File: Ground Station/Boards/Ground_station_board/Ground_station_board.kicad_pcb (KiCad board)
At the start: 4 copper layers, 59.4 x 38.2 mm, 70 parts, among them J3 USB_B_Micro, J4 SWD JST PH, J5 MICROFIT, J6 RFIO SMA, U2 SX1262, U3 PE4259 RF Switch, U4 STM32H562RGT6, U5 MIC5365-3.3YC5, U6 MIC5365-3.3YC5, U7 AS78L05RTR-E1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

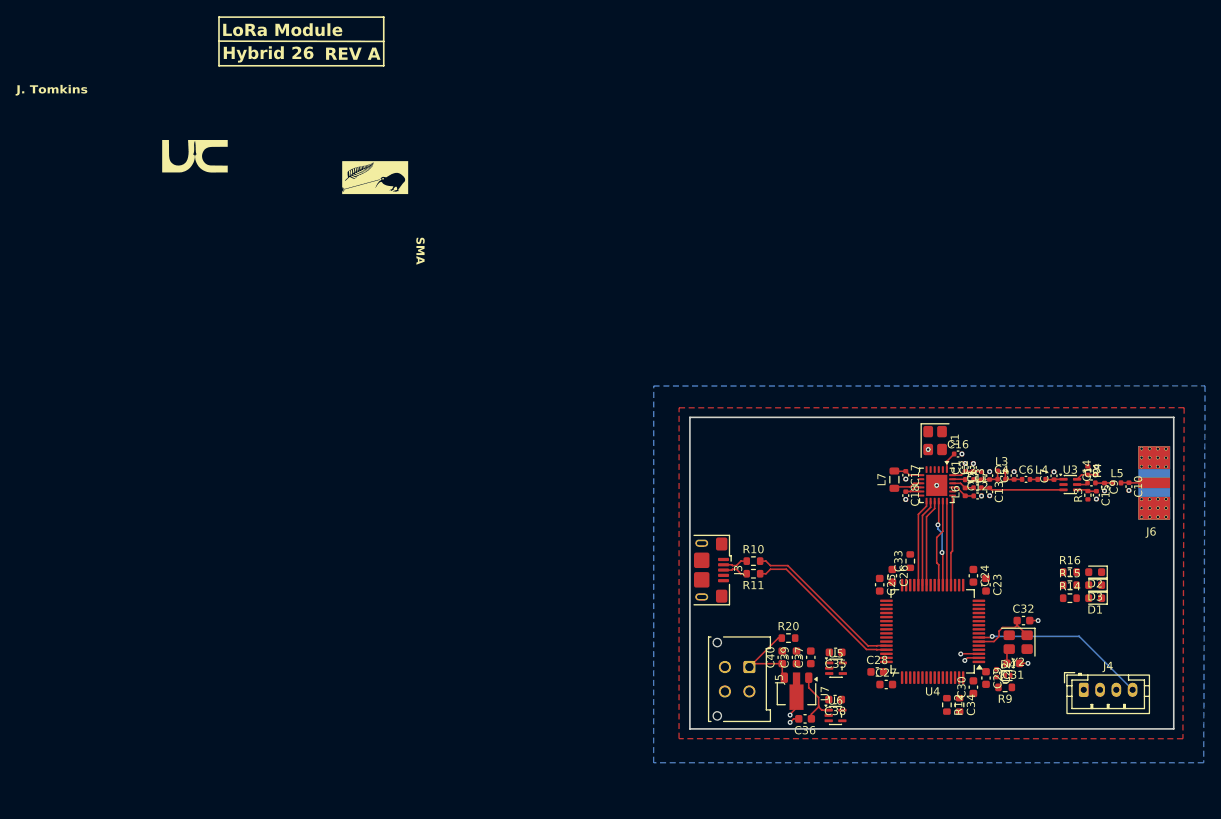
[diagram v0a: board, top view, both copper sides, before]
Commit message: via stitching added to gs board, need fencing before review
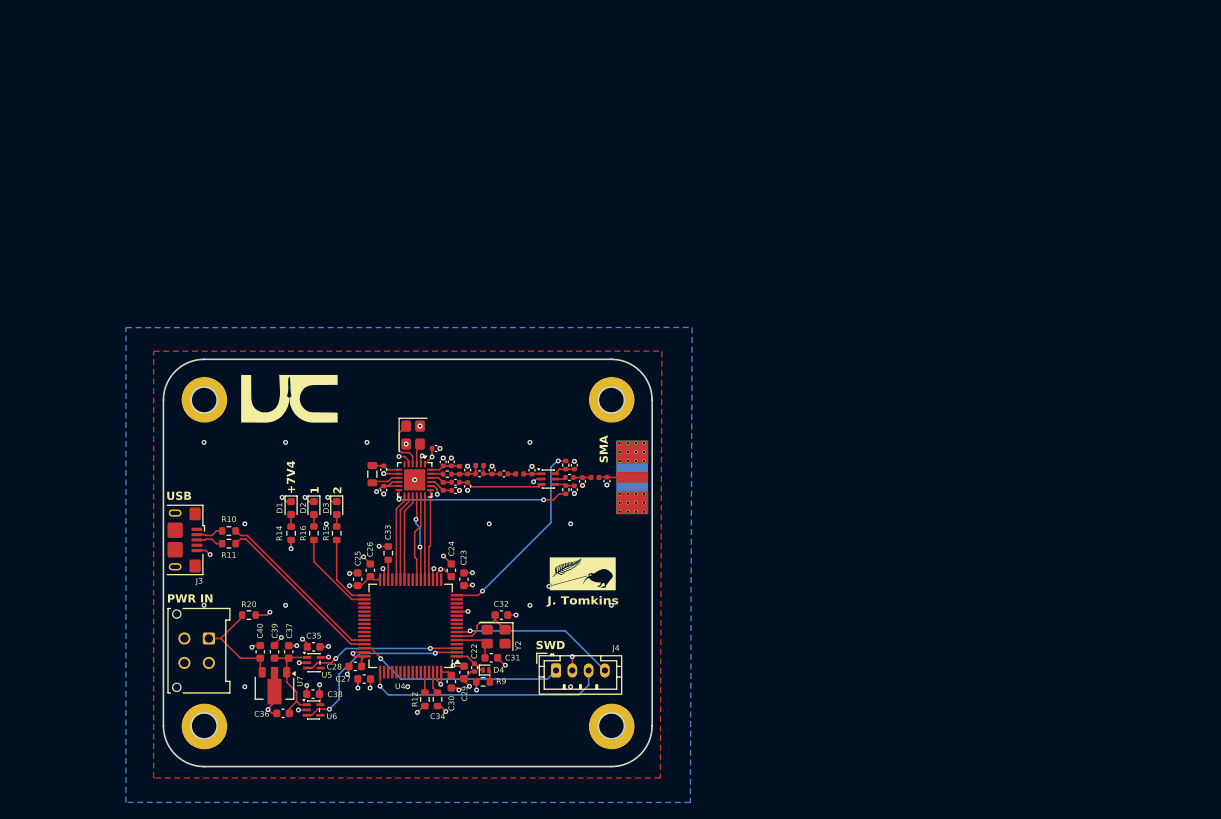
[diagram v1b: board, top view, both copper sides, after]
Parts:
- added H1: MountingHole, MountingHole:MountingHole_3.2mm_M3_DIN965_Pad, F.Cu at (125.1, 78.0)
- added H2: MountingHole, MountingHole:MountingHole_3.2mm_M3_DIN965_Pad, F.Cu at (175.1, 78.0)
- added H3: MountingHole, MountingHole:MountingHole_3.2mm_M3_DIN965_Pad, F.Cu at (125.1, 118.1)
- added H4: MountingHole, MountingHole:MountingHole_3.2mm_M3_DIN965_Pad, F.Cu at (175.1, 118.1)
- moved D1 99.3 mm to (135.7, 91.3), turned to -90 degrees
- moved D2 96.2 mm to (138.5, 91.3), turned to -90 degrees
- moved R14 95.9 mm to (135.7, 94.4), turned to 90 degrees
- moved D3 93.6 mm to (141.3, 91.3), turned to -90 degrees
- moved R16 92.9 mm to (138.5, 94.4), turned to 90 degrees
- moved R15 90.2 mm to (141.3, 94.4), turned to 90 degrees
- moved J5 66.5 mm to (125.6, 107.3)
- moved R20 66.3 mm to (130.6, 104.4)
- moved J4 64.8 mm to (168.3, 111.2)
- moved J3 64.8 mm to (121.5, 95.2)
- moved R10 64.5 mm to (128.1, 94.1)
- moved R11 64.5 mm to (128.1, 95.7)
- moved C33 64.1 mm to (147.7, 96.8)
- moved C1 64.1 mm to (154.4, 85.6)
- moved C10 64.1 mm to (174.5, 88.0)
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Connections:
- U4 pad 33: unconnected-(U4-PB12-Pad33) -> /MCU/LED1
- U4 pad 34: unconnected-(U4-PB13-Pad34) -> /MCU/LED2
- U4 pad 51: /MCU/LED2 -> unconnected-(U4-PC10-Pad51)
- U4 pad 52: /MCU/LED1 -> unconnected-(U4-PC11-Pad52)
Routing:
- net GND: track 8.12 -> 60.8 mm, vias 20 -> 65
- net /+3V3A: track 5.66 -> 44.5 mm, vias 0 -> 3
- net /MCU/SWDIO: track 0.00 -> 30.1 mm, vias 0 -> 1
- net /MCU/SWCLK: track 0.00 -> 25.6 mm, vias 0 -> 1
- net /LoRav2/ANT_SW: track 0.00 -> 24.2 mm, vias 0 -> 2
- net /LoRav2/DIO2: track 0.00 -> 22.0 mm, vias 0 -> 2
- net /MCU/3V3A_LDO_EN: track 1.86 -> 23.5 mm, vias 1 -> 2
- net /MCU/3V3_LDO_EN: track 2.24 -> 19.4 mm, vias 1 -> 2
- net +3V3: track 0.00 -> 12.3 mm, vias 0 -> 11
- net +7V4: track 0.00 -> 11.8 mm, vias 0 -> 2
- net /MCU/LED2: track 0.00 -> 10.8 mm
- net /MCU/LED1: track 0.00 -> 9.09 mm
- net /LoRav2/XTB: track 0.00 -> 6.27 mm
- net +5V: track 7.32 -> 13.2 mm
- net Net-(D4-K): track 0.00 -> 3.92 mm
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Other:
- board size 59.4 x 38.2 mm -> 60 x 50 mm
- board text added: "+7V4"
- board text added: "1"
- board text added: "2"
- board text added: "LoRa Module GS"
- board text added: "PWR IN"
- board text added: "SWD"
- board text added: "USB"
- board text removed: "LoRa Module"
